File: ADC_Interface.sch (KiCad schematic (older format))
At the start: 17 parts

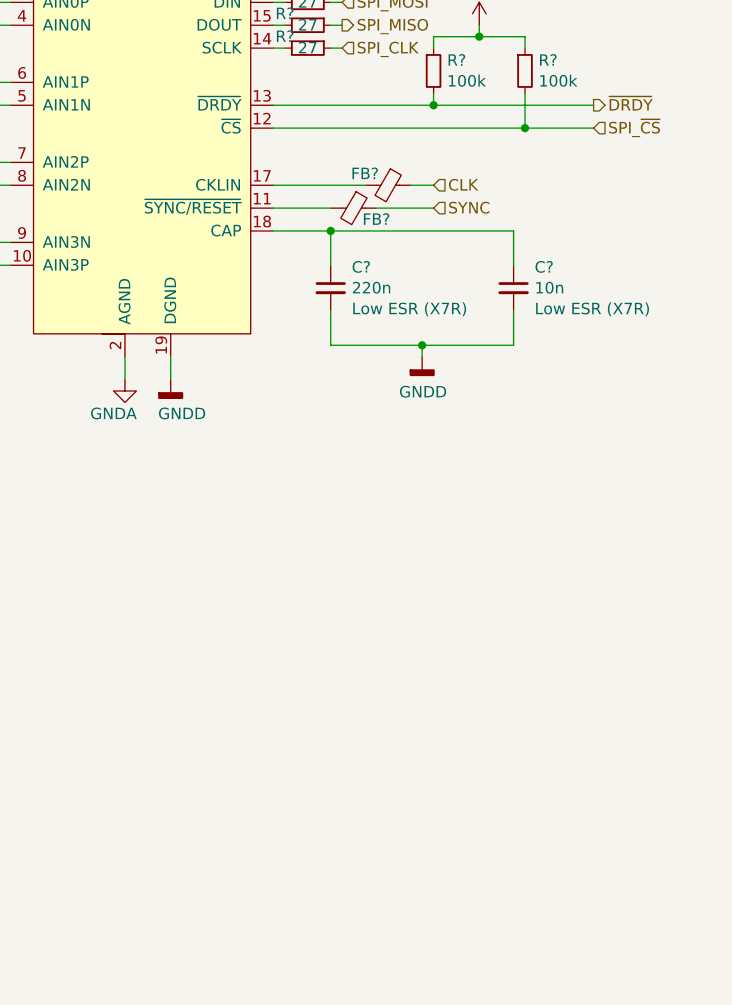
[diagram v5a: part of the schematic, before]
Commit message: Design MCU section
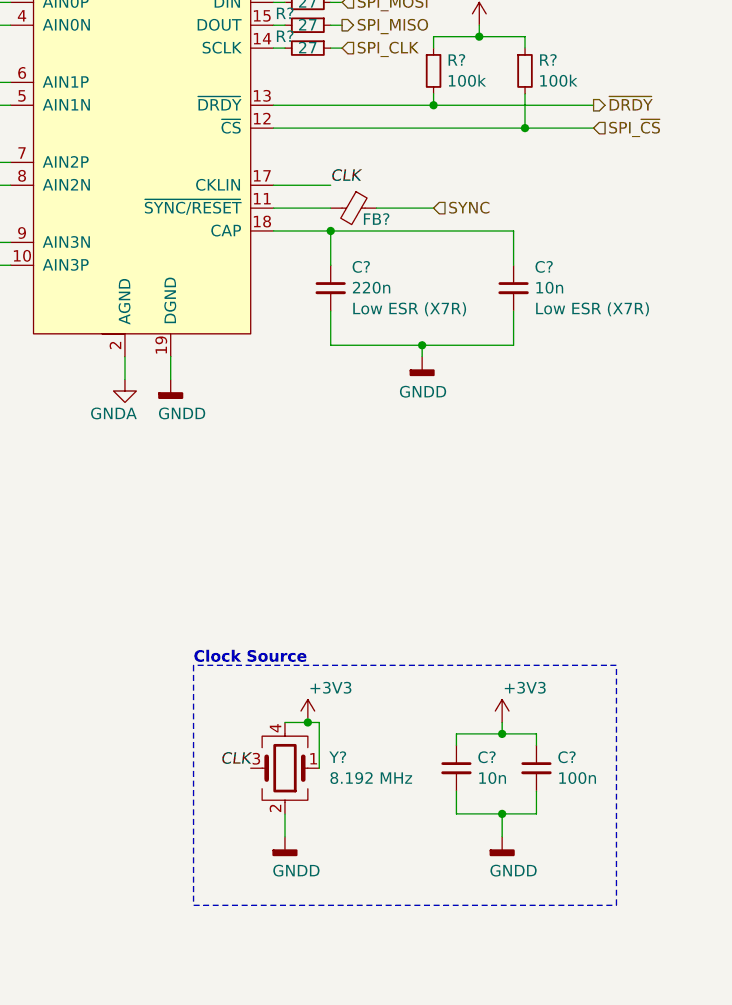
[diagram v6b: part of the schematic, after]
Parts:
- removed FB?: Ferrite_Bead_Small, symbol Device:Ferrite_Bead_Small
- added C?: 10n, symbol Device:C_Small
- added C?: 100n, symbol Device:C_Small
- added Y?: 8.192 MHz, symbol Device:Crystal_GND24
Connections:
- net +3V3: now also C?.1, C?.1, Y?.1, Y?.4
- net CLK: now also U?.17 (CKLIN), Y?.3
- net GNDD: now also C?.2, C?.2, Y?.2
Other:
- note added: "Clock Source"
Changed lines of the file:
@@
 encoding utf-8
 Sheet 3 15
-Title ""
-Date ""
-Rev ""
-Comp ""
-Comment1 ""
-Comment2 ""
+Title "Kleinvoet"
+Date "2020-06-11"
+Rev "Rev. A"
+Comp "Department of Electronic Engineering - Stellenbosch University"
+Comment1 "Author: CM Geldenhuys <20198329@sun.ac.za>"
+Comment2 "Project: Kleinvoet"
 Comment3 ""
 Comment4 ""
@@
 Wire Wire Line
 	8400 3650 8400 3550
-$Comp
-L Device:Ferrite_Bead_Small FB?
-U 1 1 5EE62B19
-P 9550 2800
-AR Path="/5EE62B19" Ref="FB?"  Part="1"
-AR Path="/5EE5ECAD/5EE62B19" Ref="FB?"  Part="1"
-F 0 "FB?" V 9500 2700 50  0000 C CNN
-F 1 "Ferrite_Bead_Small" V 9404 2800 50  0001 C CNN
-F 2 "" V 9480 2800 50  0001 C CNN
-F 3 "~" H 9550 2800 50  0001 C CNN
-	1    9550 2800
-	0    1    1    0
-$EndComp
-Wire Wire Line
-	9750 2800 9650 2800
 Wire Wire Line
 	9300 2900 9050 2900
@@
 Text HLabel 10450 2550 2    50   Input ~ 0
 SPI_~CS
-Text HLabel 9750 2800 2    50   Input ~ 0
-CLK
 Text HLabel 9750 2900 2    50   Input ~ 0
 SYNC
@@
 F1 "Sensor_Connector.sch" 50
 F2 "EN" I R 4650 4300 50
-F4 "SIG_P" I R 4650 4100 50
-F5 "SIG_N" I R 4650 4200 50
+F3 "SIG_P" I R 4650 4100 50
+F4 "SIG_N" I R 4650 4200 50
 $EndSheet
 Wire Wire Line
@@
 F1 "Sensor_Connector.sch" 50
 F2 "EN" I R 4650 4900 50
-F4 "SIG_P" I R 4650 4700 50
-F5 "SIG_N" I R 4650 4800 50
+F3 "SIG_P" I R 4650 4700 50
+F4 "SIG_N" I R 4650 4800 50
 $EndSheet
 $Sheet
@@
 F1 "Sensor_Connector.sch" 50
 F2 "EN" I R 4650 5500 50
-F4 "SIG_P" I R 4650 5300 50
-F5 "SIG_N" I R 4650 5400 50
+F3 "SIG_P" I R 4650 5300 50
+F4 "SIG_N" I R 4650 5400 50
 $EndSheet
 $Sheet
@@
 F1 "Sensor_Connector.sch" 50
 F2 "EN" I R 4650 6100 50
-F4 "SIG_P" I R 4650 5900 50
-F5 "SIG_N" I R 4650 6000 50
+F3 "SIG_P" I R 4650 5900 50
+F4 "SIG_N" I R 4650 6000 50
 $EndSheet
 Text Label 4900 4900 0    50   ~ 0
@@
 Wire Wire Line
 	800  1350 800  1500
-Wire Wire Line
-	9050 2800 9450 2800
+$Comp
+L Device:Crystal_GND24 Y?
+U 1 1 5EFB7F01
+P 9100 5350
+F 0 "Y?" H 8906 5304 50  0000 R CNN
+F 1 "8.192 MHz" H 8906 5395 50  0000 R CNN
+F 2 "" H 9100 5350 50  0001 C CNN
+F 3 "~" H 9100 5350 50  0001 C CNN
+F 4 "DSC1001CI5-008.1920" H 9100 5350 50  0001 C CNN "MPN"
+F 5 "MicroChip" H 9100 5350 50  0001 C CNN "Mfr."
+	1    9100 5350
+	-1   0    0    1
+$EndComp
+$Comp
+L power:GNDD #PWR?
+U 1 1 5EFC0262
+P 9100 5650
+AR Path="/5EFC0262" Ref="#PWR?"  Part="1"
+AR Path="/5EE5ECAD/5EFC0262" Ref="#PWR?"  Part="1"
+F 0 "#PWR?" H 9100 5400 50  0001 C CNN
+F 1 "GNDD" H 9150 5500 50  0000 C CNN
+F 2 "" H 9100 5650 50  0001 C CNN
+F 3 "" H 9100 5650 50  0001 C CNN
+	1    9100 5650
+	1    0    0    -1
+$EndComp
+Wire Wire Line
+	9100 5650 9100 5550
+Text Label 8950 5350 2    50   Italic 0
+CLK
+$Comp
+L power:+3V3 #PWR?
+U 1 1 5EFCE017
+P 9200 5150
+AR Path="/5EFCE017" Ref="#PWR?"  Part="1"
+AR Path="/5EE5ECAD/5EFCE017" Ref="#PWR?"  Part="1"
+F 0 "#PWR?" H 9200 5000 50  0001 C CNN
+F 1 "+3V3" H 9300 5300 50  0000 C CNN
+F 2 "" H 9200 5150 50  0001 C CNN
+F 3 "" H 9200 5150 50  0001 C CNN
+	1    9200 5150
+	1    0    0    -1
+$EndComp
+Wire Wire Line
+	9200 5150 9100 5150
+Wire Wire Line
+	9200 5150 9250 5150
+Wire Wire Line
+	9250 5150 9250 5350
+Connection ~ 9200 5150
+$Comp
+L Device:C_Small C?
+U 1 1 5EFD75E4
+P 9850 5350
+F 0 "C?" H 9942 5396 50  0000 L CNN
+F 1 "10n" H 9942 5305 50  0000 L CNN
+F 2 "" H 9850 5350 50  0001 C CNN
+F 3 "~" H 9850 5350 50  0001 C CNN
+	1    9850 5350
+	1    0    0    -1
+$EndComp
+$Comp
+L Device:C_Small C?
+U 1 1 5EFD77FC
+P 10200 5350
+F 0 "C?" H 10292 5396 50  0000 L CNN
+F 1 "100n" H 10292 5305 50  0000 L CNN
+F 2 "" H 10200 5350 50  0001 C CNN
+F 3 "~" H 10200 5350 50  0001 C CNN
+	1    10200 5350
+	1    0    0    -1
+$EndComp
+$Comp
+L power:+3V3 #PWR?
+U 1 1 5EFD7DB7
+P 10050 5150
+AR Path="/5EFD7DB7" Ref="#PWR?"  Part="1"
+AR Path="/5EE5ECAD/5EFD7DB7" Ref="#PWR?"  Part="1"
+F 0 "#PWR?" H 10050 5000 50  0001 C CNN
+F 1 "+3V3" H 10150 5300 50  0000 C CNN
+F 2 "" H 10050 5150 50  0001 C CNN
+F 3 "" H 10050 5150 50  0001 C CNN
+	1    10050 5150
+	1    0    0    -1
+$EndComp
+$Comp
+L power:GNDD #PWR?
+U 1 1 5EFD831E
+P 10050 5650
+AR Path="/5EFD831E" Ref="#PWR?"  Part="1"
+AR Path="/5EE5ECAD/5EFD831E" Ref="#PWR?"  Part="1"
+F 0 "#PWR?" H 10050 5400 50  0001 C CNN
+F 1 "GNDD" H 10100 5500 50  0000 C CNN
+F 2 "" H 10050 5650 50  0001 C CNN
+F 3 "" H 10050 5650 50  0001 C CNN
+	1    10050 5650
+	1    0    0    -1
+$EndComp
+Wire Wire Line
+	10050 5650 10050 5550
+Wire Wire Line
+	10050 5550 10200 5550
+Wire Wire Line
+	10200 5550 10200 5450
+Wire Wire Line
+	10050 5550 9850 5550
+Wire Wire Line
+	9850 5550 9850 5450
+Connection ~ 10050 5550
+Wire Wire Line
+	9850 5250 9850 5200
+Wire Wire Line
+	9850 5200 10050 5200
+Wire Wire Line
+	10050 5200 10050 5150
+Wire Wire Line
+	10200 5250 10200 5200
+Wire Wire Line
+	10200 5200 10050 5200
+Connection ~ 10050 5200
+Wire Notes Line
+	8700 5950 10550 5950
+Wire Notes Line
+	10550 5950 10550 4900
+Wire Notes Line
+	10550 4900 8700 4900
+Wire Notes Line
+	8700 4900 8700 5950
+Text Notes 8700 4900 0    50   ~ 10
+Clock Source
+Text Label 9300 2800 0    50   Italic 0
+CLK
+Wire Wire Line
+	9300 2800 9050 2800
 $EndSCHEMATC

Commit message: Finalise design
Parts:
- added J?: ADC_SPI_CONN, symbol Connector_Generic:Conn_01x05
- added TP?: TestPoint, symbol Connector:TestPoint
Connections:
- net GND: now also J?.1 (Pin_1)
- net SPI_CLK: now also J?.3 (Pin_3)
- net SPI_MISO: now also J?.4 (Pin_4)
- net SPI_MOSI: now also J?.5 (Pin_5)
- net SYNC: now also TP?.1
- net ~DRDY: now also J?.2 (Pin_2)
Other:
- note added: "SPI Conn"
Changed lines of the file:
@@
 $Descr A4 11693 8268
 encoding utf-8
-Sheet 3 15
+Sheet 2 15
 Title "Kleinvoet"
 Date "2020-06-11"
@@
 	9300 2900 9050 2900
 Wire Wire Line
-	9750 2900 9500 2900
+	9750 2900 9700 2900
 $Comp
 L Device:C_Small C?
@@
 F5 "AIN_N" I L 6150 4200 50
 $EndSheet
-$Comp
-L Device:R_Small R?
-U 1 1 5EE62BDA
-P 10150 2300
-AR Path="/5EE62BDA" Ref="R?"  Part="1"
-AR Path="/5EE5ECAD/5EE62BDA" Ref="R?"  Part="1"
-F 0 "R?" H 10209 2346 50  0000 L CNN
-F 1 "100k" H 10209 2255 50  0000 L CNN
-F 2 "" H 10150 2300 50  0001 C CNN
-F 3 "~" H 10150 2300 50  0001 C CNN
-	1    10150 2300
-	1    0    0    -1
-$EndComp
 Wire Wire Line
 	9750 2450 9050 2450
@@
 $EndComp
 Wire Wire Line
-	10150 2200 10150 2150
-Wire Wire Line
-	10150 2150 9950 2150
-Wire Wire Line
 	9950 2150 9950 2100
 Wire Wire Line
@@
 Wire Wire Line
 	9750 2150 9950 2150
-Connection ~ 9950 2150
 Wire Wire Line
 	9750 2450 9750 2400
@@
 Wire Wire Line
 	9300 2800 9050 2800
+Connection ~ 9950 2150
+Wire Wire Line
+	10150 2150 9950 2150
+Wire Wire Line
+	10150 2200 10150 2150
+$Comp
+L Device:R_Small R?
+U 1 1 5EE62BDA
+P 10150 2300
+AR Path="/5EE62BDA" Ref="R?"  Part="1"
+AR Path="/5EE5ECAD/5EE62BDA" Ref="R?"  Part="1"
+F 0 "R?" H 10209 2346 50  0000 L CNN
+F 1 "100k" H 10209 2255 50  0000 L CNN
+F 2 "" H 10150 2300 50  0001 C CNN
+F 3 "~" H 10150 2300 50  0001 C CNN
+	1    10150 2300
+	1    0    0    -1
+$EndComp
+$Comp
+L Connector_Generic:Conn_01x05 J?
+U 1 1 5EFF03C2
+P 1350 3250
+F 0 "J?" H 1268 2825 50  0000 C CNN
+F 1 "ADC_SPI_CONN" H 1268 2916 50  0000 C CNN
+F 2 "" H 1350 3250 50  0001 C CNN
+F 3 "~" H 1350 3250 50  0001 C CNN
+	1    1350 3250
+	-1   0    0    1
+$EndComp
+Text HLabel 1800 3050 2    50   Input ~ 0
+SPI_MOSI
+Wire Wire Line
+	1800 3050 1550 3050
+Text HLabel 1800 3150 2    50   Output ~ 0
+SPI_MISO
+Text HLabel 1800 3350 2    50   Output ~ 0
+~DRDY
+$Comp
+L Connector:TestPoint TP?
+U 1 1 5EFF8206
+P 9700 2900
+F 0 "TP?" H 9758 2972 50  0000 L CNN
+F 1 "TestPoint" H 9758 2927 50  0001 L CNN
+F 2 "" H 9900 2900 50  0001 C CNN
+F 3 "~" H 9900 2900 50  0001 C CNN
+	1    9700 2900
+	1    0    0    -1
+$EndComp
+Connection ~ 9700 2900
+Wire Wire Line
+	9700 2900 9500 2900
+$Comp
+L power:GND #PWR?
+U 1 1 5EFFED1A
+P 1800 3500
+F 0 "#PWR?" H 1800 3250 50  0001 C CNN
+F 1 "GND" H 1805 3327 50  0000 C CNN
+F 2 "" H 1800 3500 50  0001 C CNN
+F 3 "" H 1800 3500 50  0001 C CNN
+	1    1800 3500
+	1    0    0    -1
+$EndComp
+Wire Wire Line
+	1800 3500 1800 3450
+Wire Wire Line
+	1800 3450 1550 3450
+Wire Wire Line
+	1800 3350 1550 3350
+Wire Wire Line
+	1800 3250 1550 3250
+Wire Wire Line
+	1800 3150 1550 3150
+Wire Notes Line
+	1050 2700 2300 2700
+Wire Notes Line
+	2300 2700 2300 3750
+Wire Notes Line
+	2300 3750 1050 3750
+Wire Notes Line
+	1050 2700 1050 3750
+Text Notes 1050 2700 0    50   ~ 10
+SPI Conn
+Text HLabel 1800 3250 2    50   Input ~ 0
+SPI_CLK
 $EndSCHEMATC

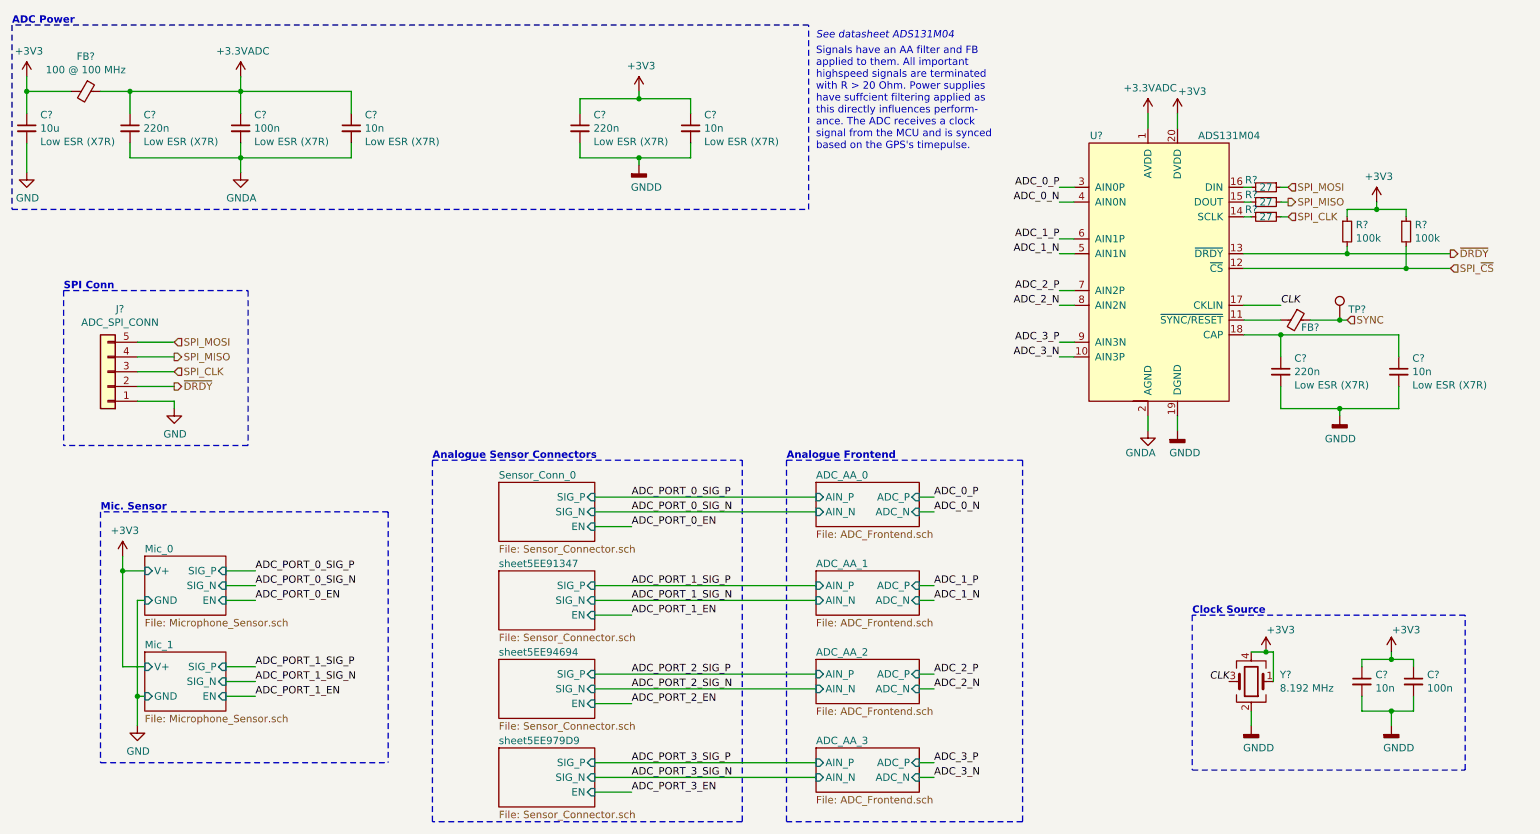
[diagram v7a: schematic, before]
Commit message: Add PWR Flags
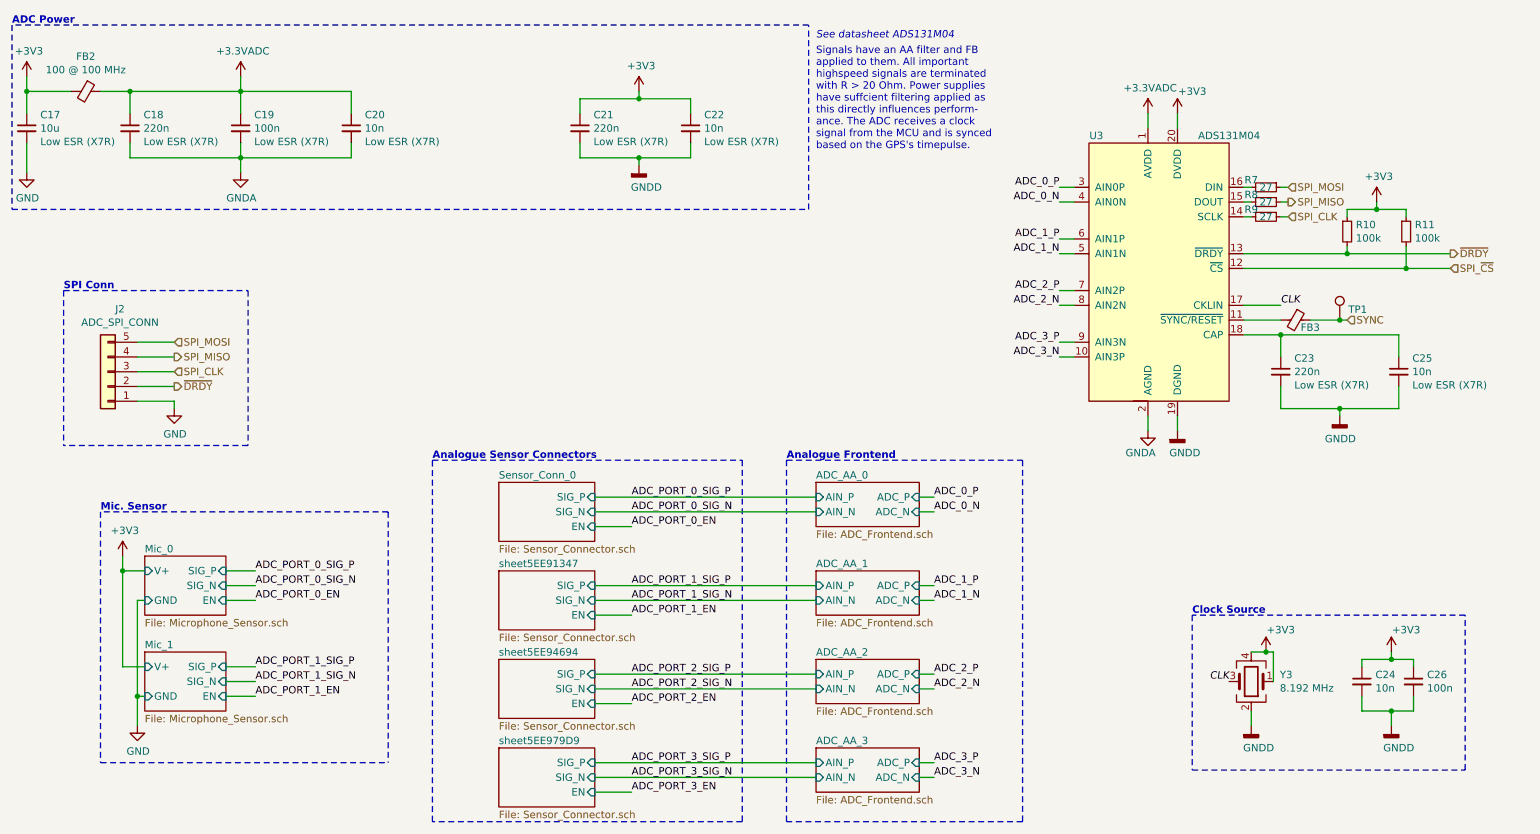
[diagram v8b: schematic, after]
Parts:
- gave numbers to parts that had none: 21
